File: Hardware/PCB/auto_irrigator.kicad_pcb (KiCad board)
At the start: 2 copper layers, 73.2 x 43.9 mm, 51 parts, among them J1 GND 12V, J10 FLOW3, J2 VALVE1, J3 VALVE2, J4 VALVE3, J5 VALVE4, J6 I2C1, J7 FLOW4, J8 FLOW1, J9 FLOW2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

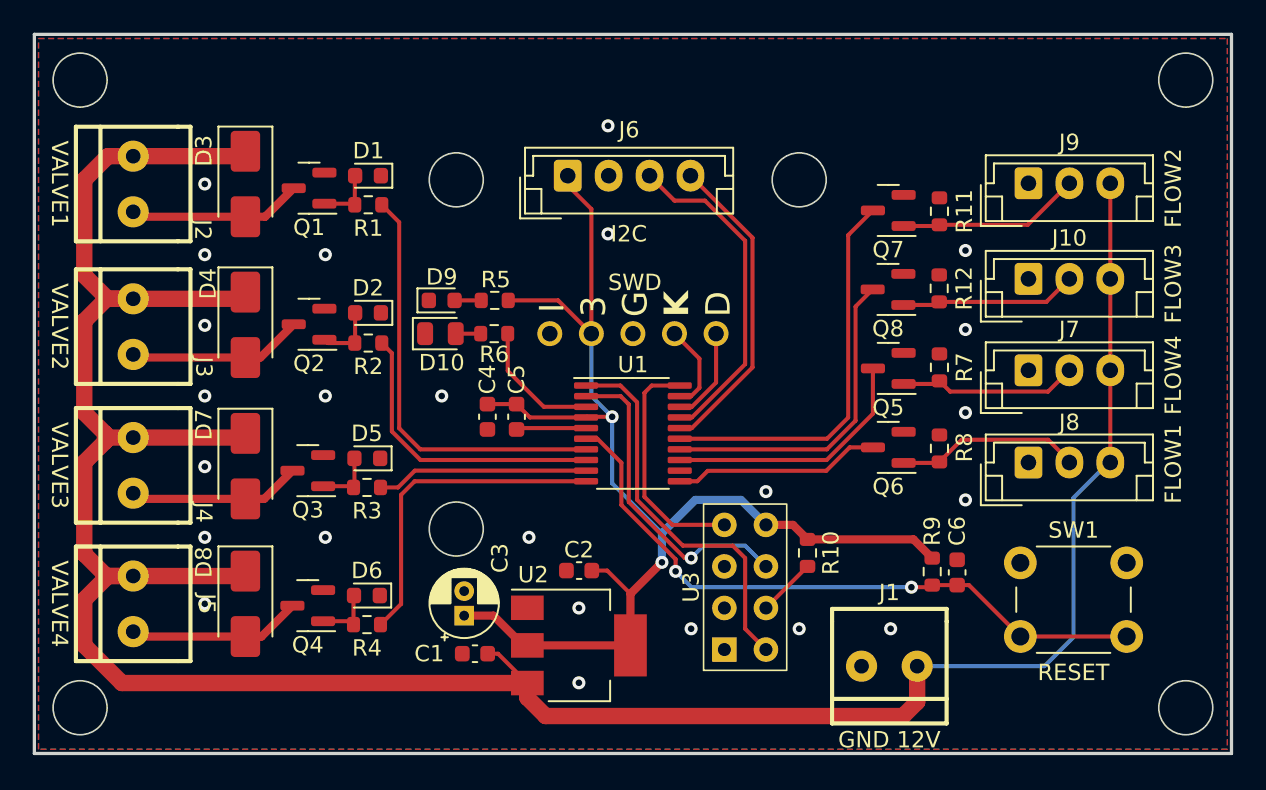
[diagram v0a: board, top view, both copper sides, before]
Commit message: AutoIrrigator rev 2
Aggiunte notifiche. Migliorata ulteriormente la stabilità. Modificata PCB per sistemare gli errori della rev 1.
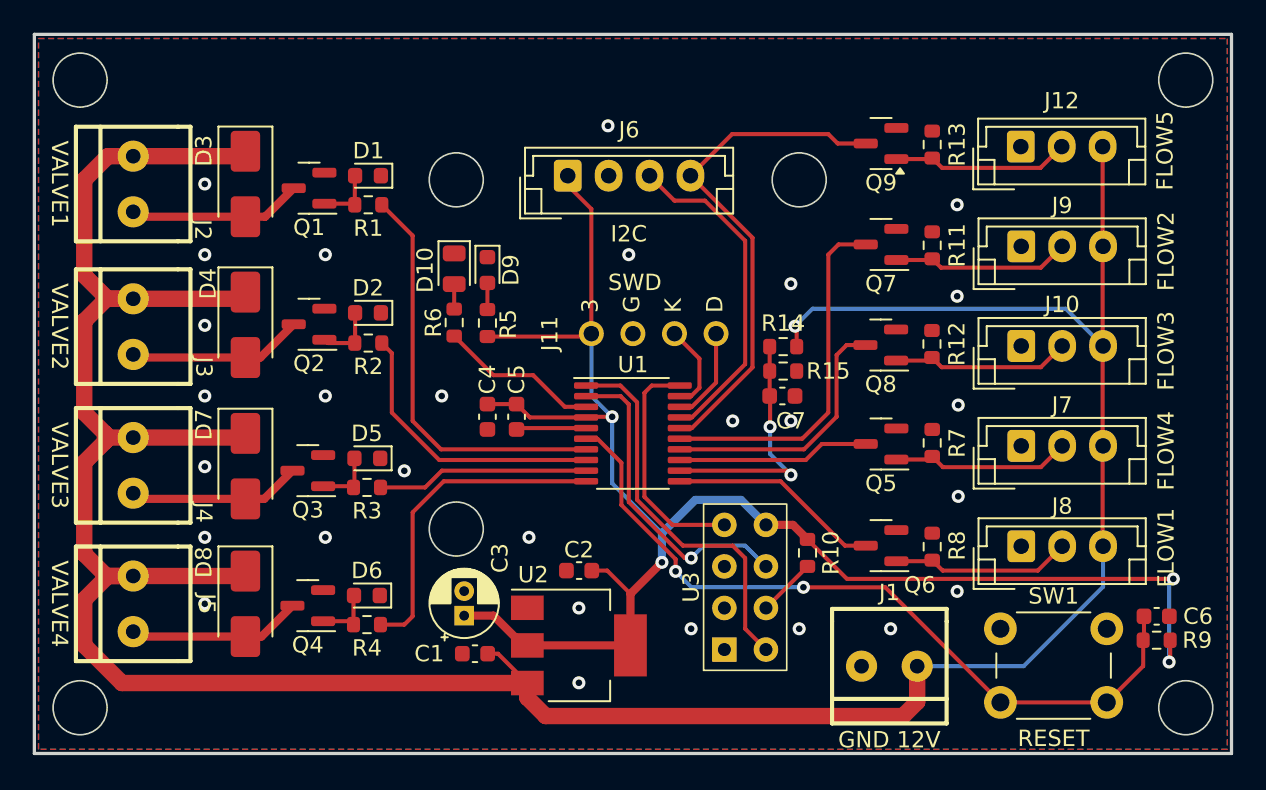
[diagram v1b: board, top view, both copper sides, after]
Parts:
- removed P1: ~, power_symbols:stm_headers
- added C7: 100nF, Capacitor_SMD:C_0603_1608Metric, F.Cu at (178.5, 80.3)
- added J11: ~, headers:swdio, F.Cu at (166.9, 76.5)
- added J12: FLOW5, Connector_JST:JST_EH_B3B-EH-A_1x03_P2.50mm_Vertical, F.Cu at (193.1, 65.0)
- added Q9: AO3400A, Package_TO_SOT_SMD:SOT-23, F.Cu at (184.6, 64.8)
- added R13: 10K, Resistor_SMD:R_0603_1608Metric, F.Cu at (187.7, 64.9)
- added R14: 5K1, Resistor_SMD:R_0603_1608Metric, F.Cu at (178.6, 77.2)
- added R15: 1K8, Resistor_SMD:R_0603_1608Metric, F.Cu at (178.6, 78.7)
- moved R9 14.3 mm to (201.4, 95.2), turned to 180 degrees
- moved C6 12.5 mm to (201.4, 93.7), turned to 0 degrees
- moved Q6 6.02 mm to (184.6, 89.4)
- moved R8 6.02 mm to (187.7, 89.5)
- moved J8 5.14 mm to (193.1, 89.4)
- moved J7 4.64 mm to (193.1, 83.3)
- moved Q5 4.64 mm to (184.6, 83.2)
- moved R7 4.64 mm to (187.7, 83.1)
- moved SW1 4.21 mm to (191.9, 94.5)
- moved J10 4.12 mm to (193.1, 77.2)
- moved D10 4.05 mm to (158.5, 72.5), turned to -90 degrees
- moved J9 3.88 mm to (193.1, 71.1)
- moved Q8 3.43 mm to (184.6, 77.2)
- moved R12 3.43 mm to (187.7, 77.1)
- moved D9 3.35 mm to (160.5, 72.6), turned to -90 degrees
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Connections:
- net SCL renamed FLOW5
- U1 pad 12: unconnected-(U1-PA5-Pad12) -> BAT_ADC
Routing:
- net +12V: track 169.3 -> 192.2 mm, vias 0 -> 1
- net +3V3: track 80.3 -> 102.6 mm, vias 2 -> 4
- net BAT_ADC: track 0.00 -> 15.3 mm, vias 0 -> 2
- net FLOW5: track 19.3 -> 31.3 mm
- net Net-(J12-Pin_2): track 0.00 -> 10.9 mm
- net STMNRST: track 40.1 -> 46.6 mm
- net FLOW4: track 15.7 -> 11.8 mm
- net FLOW3: track 19.9 -> 16.2 mm
- net FLOW2: track 24.1 -> 21.9 mm
- net STATUS: track 7.97 -> 9.85 mm
- net VALVE1: track 26.1 -> 25.3 mm
- net VALVE2: track 18.2 -> 17.6 mm
- net GND: vias 24 -> 27
- net (no net): vias 0 -> 1
